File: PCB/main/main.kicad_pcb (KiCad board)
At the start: 2 copper layers, 17 x 63.7 mm, 10 parts, among them J1 Conn_01x06_Pin, J2 Conn_01x05_Pin, J3 Conn_01x05_Pin, J4 Conn_01x06_Pin, J5 Conn_01x06_Pin, U1 ATtiny1614-SS, U2 TB6612FNG

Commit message: PCB Nearly Complete
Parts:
- removed C1: C, Capacitor_SMD:C_1206_3216Metric_Pad1.33x1.80mm_HandSolder
- removed J3: Conn_01x05_Pin, Connector_PinHeader_2.54mm:PinHeader_1x05_P2.54mm_Vertical
- removed J4, J5: Conn_01x06_Pin, Connector_PinHeader_2.54mm:PinHeader_1x06_P2.54mm_Vertical
- removed U2: TB6612FNG, Package_SO:SSOP-24_5.3x8.2mm_P0.65mm
- added C3: 10uF, PCM_JLCPCB:C_0805, F.Cu at (146.6, 136.4)
- added C4: 10uF, PCM_JLCPCB:C_0805, F.Cu at (137.9, 133.8)
- added C5: 100nF, PCM_JLCPCB:C_0402, F.Cu at (139.8, 132.5)
- added C7: 100nF, PCM_JLCPCB:C_0402, F.Cu at (138.6, 86.2)
- added C8: 100nF, PCM_JLCPCB:C_0402, F.Cu at (144.3, 91.5)
- added D3: APA-106-F5, LED_THT:LED_D5.0mm-4_RGB, F.Cu at (144.1, 84.0)
- added J6: Conn_01x05, Connector_JST:JST_XH_B5B-XH-AM_1x05_P2.50mm_Vertical, F.Cu at (137.2, 100.0)
- added R1: 10kΩ, PCM_JLCPCB:R_0402, F.Cu at (136.5, 133.0)
- added R2: 470Ω, PCM_JLCPCB:R_0402, F.Cu at (138.1, 85.0)
- added S1: Tactile Button, 160gf, PCM_JLCPCB:SW_TS-1088-AR02016, F.Cu at (147.9, 129.0)
- added S2: Tactile Button, 160gf, PCM_JLCPCB:SW_TS-1088-AR02016, F.Cu at (136.5, 129.0)
- added U5: L9110, L9110:so-8, F.Cu at (142.2, 136.6)
- added U7: ~, EasyEDA_Lib:SOT-23-6_L2.9-W1.6-P0.95-LS2.9-BL, F.Cu at (142.2, 92.2)
- C2: value C -> 100nF; footprint Capacitor_SMD:C_1206_3216Metric_Pad1.33x1.80mm_HandSolder -> PCM_JLCPCB:C_0402
- J1: value Conn_01x06_Pin -> Conn_01x05; footprint Connector_PinHeader_2.54mm:PinHeader_1x06_P2.54mm_Vertical -> Connector_JST:JST_XH_B5B-XH-AM_1x05_P2.50mm_Vertical; moved to F.Cu
- U1: value ATtiny1614-SS -> ~; footprint Package_SO:SOIC-14_3.9x8.7mm_P1.27mm -> EasyEDA_Lib:TSSOP-20_L6.5-W4.4-P0.65-LS6.4-BL
- U3: footprint Motorized Fader:MF60T -> Faders:MF60T-MF100T
- moved J2 22.3 mm to (137.1, 122.5)
- moved C2 11.0 mm to (148.4, 125.6), turned to 0 degrees
- moved U1 6.71 mm to (142.2, 128.6), turned to -90 degrees
- moved J1 1.12 mm to (148.2, 100.0), turned to -90 degrees
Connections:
- C2 pad 1: Vin -> NRST
- J1 pad 2: Vin -> VMOT
- J1 pad 3: Vcc -> +5V
- J1 pad 4: SDA -> RX_UP
- J1 pad 5: SCL -> TX_UP
- J2 pad 1: GND -> +5V
- J2 pad 2: Vin -> SWD
- J2 pad 3: LED_R -> SWC
- J2 pad 4: LED_G -> GND
- J2 pad 5: LED_B -> NRST
- U1 pad 1: Vcc -> TX_UP
- U1 pad 10: UPDI -> SWD
- U1 pad 11: M1 -> SWC
- U1 pad 12: M2 -> unconnected-(U1-PB5-Pad12)
- U1 pad 13: LED_B -> unconnected-(U1-PB6-Pad13)
- U1 pad 14: GND -> unconnected-(U1-PB7-Pad14)
- U1 pad 2: MPWM -> RX_UP
- U1 pad 3: LED_G -> Wiper
- U1 pad 4: Wiper -> RGB_DIN
- U1 pad 5: Touch -> M1
- U1 pad 6: UART_RX -> M2
- U1 pad 7: LED_R -> GND
- U1 pad 8: SDA -> unconnected-(U1-PA12-Pad8)
- U1 pad 9: SCL -> +5V
- U3 pad 2: Vcc -> +5V
- U3 pad 5: Touch -> Fader_Touch
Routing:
- net GND: track 130.6 -> 25.4 mm, vias 6 -> 88
- net Vin: track 100.1 -> 0.00 mm, vias 2 -> 0
- net Vcc: track 87.1 -> 0.00 mm, vias 2 -> 0
- net +5V: track 0.00 -> 79.2 mm
- net VMOT: track 0.00 -> 61.1 mm, vias 0 -> 1
- net SCL: track 57.7 -> 0.00 mm, vias 2 -> 0
- net SDA: track 53.1 -> 0.00 mm, vias 2 -> 0
- net RGB_DIN: track 0.00 -> 45.6 mm, vias 0 -> 2
- net Motor-: track 4.16 -> 42.6 mm
- net Motor+: track 7.73 -> 42.6 mm
- net LED_B: track 29.1 -> 0.00 mm, vias 1 -> 0
- net LED_R: track 27.2 -> 0.00 mm, vias 1 -> 0
- net TX_DOWN: track 0.00 -> 23.4 mm
- net RX_UP: track 0.00 -> 23.1 mm, vias 0 -> 1
- net LED_G: track 22.3 -> 0.00 mm, vias 1 -> 0
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- added copper zone on B.Cu, net GND
- added copper zone on F.Cu, net GND
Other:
- board size 17 x 63.7 mm -> 17 x 101.3 mm

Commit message: PCB Updates
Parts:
- added J3: Boot Pin, Connector_PinHeader_2.54mm:PinHeader_1x01_P2.54mm_Vertical, B.Cu at (149.3, 117.5)
- J1, J6: moved to B.Cu
- moved J6 10.0 mm to (137.2, 110.0), turned to 90 degrees
- moved J1 9.95 mm to (148.2, 110.0), turned to 90 degrees
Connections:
- J1 pad 1: GND -> TX_UP
- J1 pad 2: VMOT -> RX_UP
- J1 pad 4: RX_UP -> VMOT
- J1 pad 5: TX_UP -> GND
- J6 pad 1: GND -> RX_DOWN
- J6 pad 2: VMOT -> TX_DOWN
- J6 pad 4: TX_DOWN -> VMOT
- J6 pad 5: RX_DOWN -> GND
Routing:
- net BOOT_BTN: track 13.9 -> 28.5 mm
- net GND: vias 88 -> 102
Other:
- board text added: "+5V"
- board text added: "5V"
- board text added: "Boot"
- board text added: "DIN"
- board text added: "DOUT"
- board text added: "Down"
- board text added: "Ground"
- board text added: "Pot"
- board text added: "RST"
- board text added: "Reset"
- board text added: "SWD Clock"
- board text added: "SWD Data"
- board text added: "Touch"
- board text added: "Up"
- board text added: "V Mot"

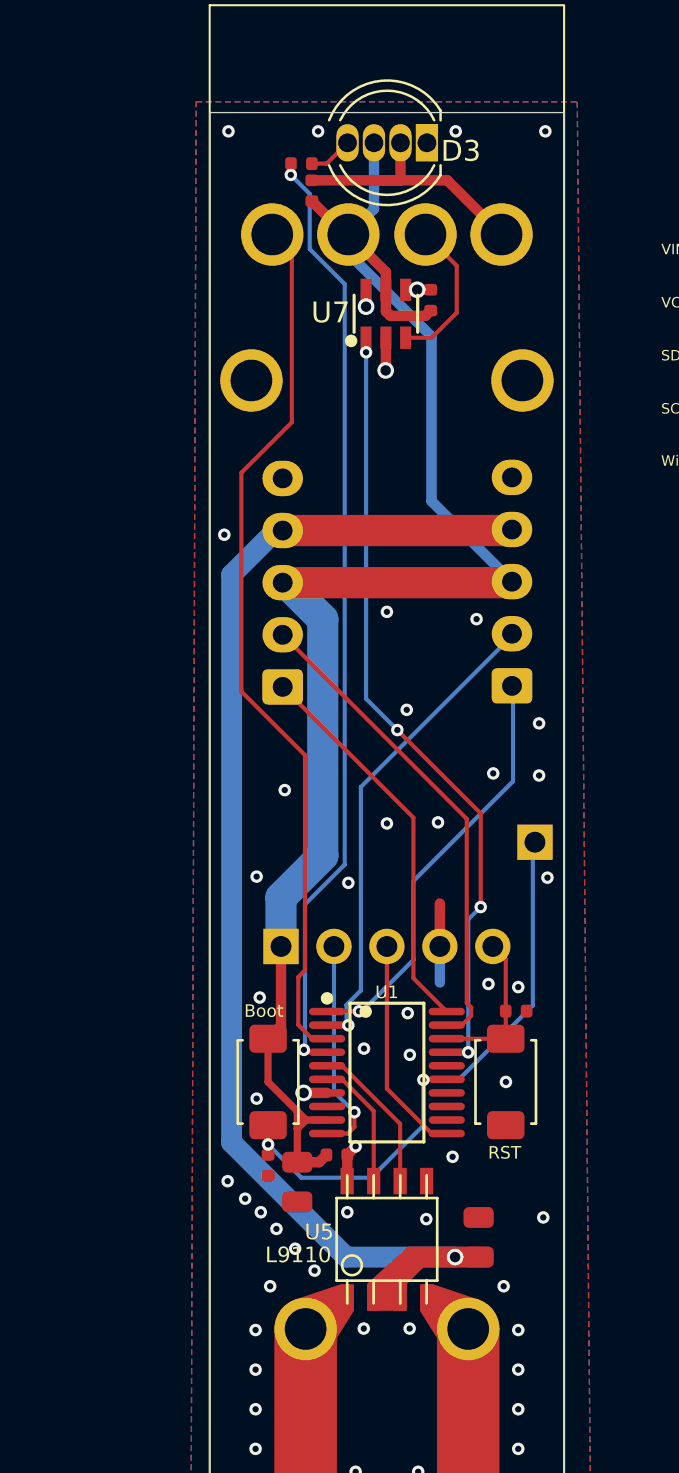
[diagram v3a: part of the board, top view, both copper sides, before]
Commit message: Progress on PCB
Flipped side of board for components
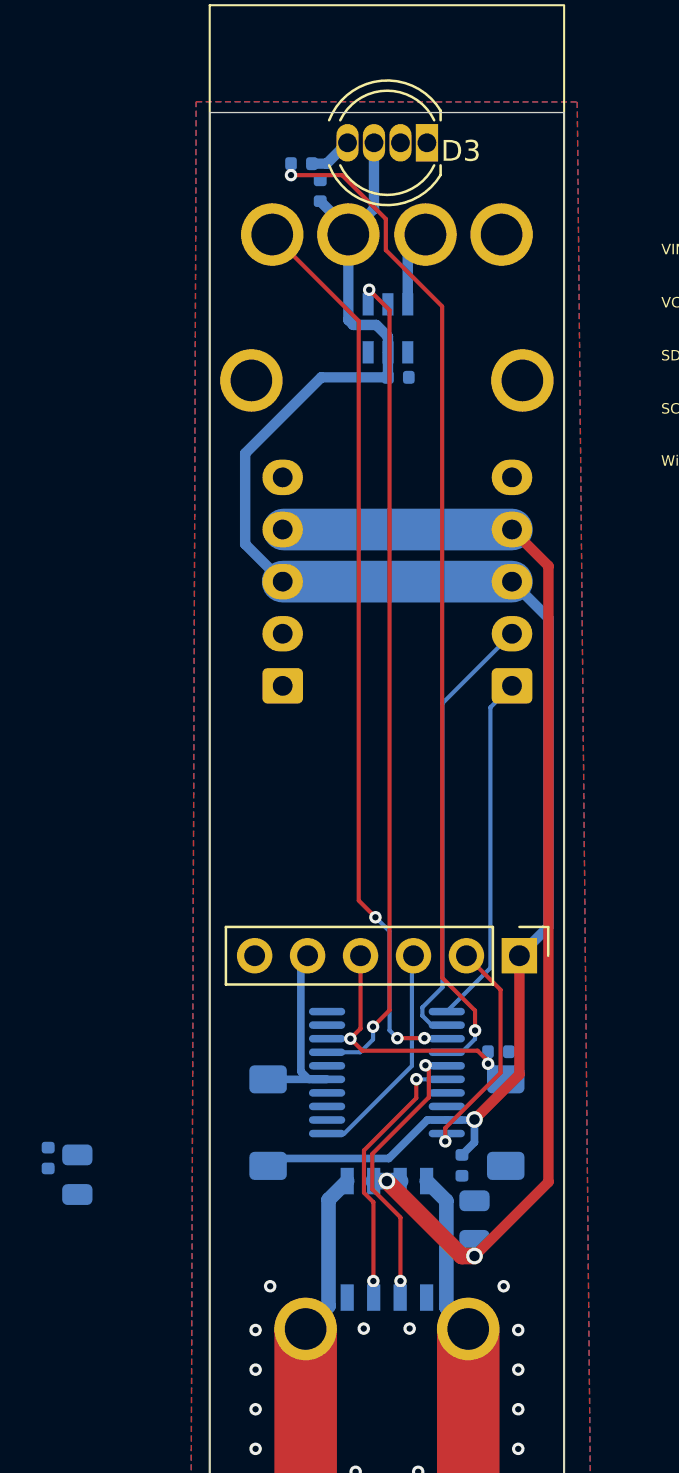
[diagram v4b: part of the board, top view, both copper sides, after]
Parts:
- removed J2: Conn_01x05_Pin, Connector_PinHeader_2.54mm:PinHeader_1x05_P2.54mm_Vertical
- removed J3: Boot Pin, Connector_PinHeader_2.54mm:PinHeader_1x01_P2.54mm_Vertical
- added J4: Conn_01x06_Pin, Connector_PinHeader_2.54mm:PinHeader_1x06_P2.54mm_Vertical, F.Cu at (148.6, 122.9)
- C2, C3, C4, C5, C7, C8, R1, R2, S1, S2, U1, U5, U7: moved to B.Cu
- moved C4 10.6 mm to (127.3, 133.4)
- moved R1 10.6 mm to (126.0, 132.7)
- moved C5 6.02 mm to (145.8, 133.0), turned to -90 degrees
- moved C8 4.01 mm to (142.8, 95.2), turned to 0 degrees
- moved C2 2.13 mm to (147.6, 127.5)
- moved S1 1.95 mm to (147.9, 130.9)
- moved S2 1.95 mm to (136.5, 130.9), turned to 90 degrees
- moved C3 0.82 mm to (146.4, 135.7)
- moved U7 0.71 mm to (142.2, 92.8)
- moved C7 0.40 mm to (139.0, 86.2)
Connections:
- net BOOT_BTN renamed BOOT
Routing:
- net GND: track 25.4 -> 0.00 mm, vias 102 -> 62
- net TX_DOWN: track 23.4 -> 0.00 mm
- net RX_DOWN: track 18.8 -> 0.00 mm
- net BOOT: track 28.5 -> 9.93 mm, vias 2 -> 0
- net M2: track 6.23 -> 13.2 mm, vias 0 -> 2
- net M1: track 7.41 -> 13.9 mm, vias 0 -> 2
- net NRST: track 7.51 -> 13.8 mm, vias 0 -> 2
- net VMOT: track 61.6 -> 55.8 mm, vias 1 -> 2
- net Motor-: track 42.6 -> 47.9 mm
- net Motor+: track 42.6 -> 47.9 mm
- net Fader_Touch: track 7.32 -> 3.70 mm
- net TX_UP: track 20.2 -> 16.9 mm, vias 1 -> 0
- net +5V: track 79.2 -> 82.4 mm, vias 0 -> 1
- net RGB_DIN: track 45.6 -> 48.7 mm
- net Touch: track 37.8 -> 39.9 mm, vias 4 -> 2
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
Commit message: PCB Progress
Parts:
- moved C4 22.1 mm to (147.9, 125.4), turned to 180 degrees
- moved R1 12.8 mm to (136.4, 125.4), turned to 90 degrees
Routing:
- net TX_DOWN: track 0.00 -> 21.5 mm, vias 0 -> 1
- net GND: track 0.00 -> 21.1 mm, vias 62 -> 109
- net RX_DOWN: track 0.00 -> 16.8 mm
- net BOOT: track 9.93 -> 12.9 mm
- net NRST: track 13.8 -> 14.4 mm
- net +5V: track 82.4 -> 82.0 mm, vias 1 -> 2

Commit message: PCB Final Draft
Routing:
- net GND: vias 109 -> 113
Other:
- board text removed: "B"
- board text removed: "G"
- board text removed: "R"
- board text removed: "SCL"
- board text removed: "SDA"
- board text removed: "UPDI"
- board text removed: "VCC"
- board text removed: "VIN"
- board text removed: "Wiper"
